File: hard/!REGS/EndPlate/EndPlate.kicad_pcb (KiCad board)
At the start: 2 copper layers, 99.1 x 68.6 mm, 39 parts, among them J1 Conn_01x13_Socket, J10 Conn_01x03_Pin, J11 Conn_01x09_Pin, J12 Conn_01x09_Pin, J13 Conn_01x09_Pin, J14 Conn_01x09_Pin, J15 Conn_01x01_Pin, J16 Conn_01x01_Pin, J17 Screw_Terminal_01x02, J2 Conn_01x13_Socket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

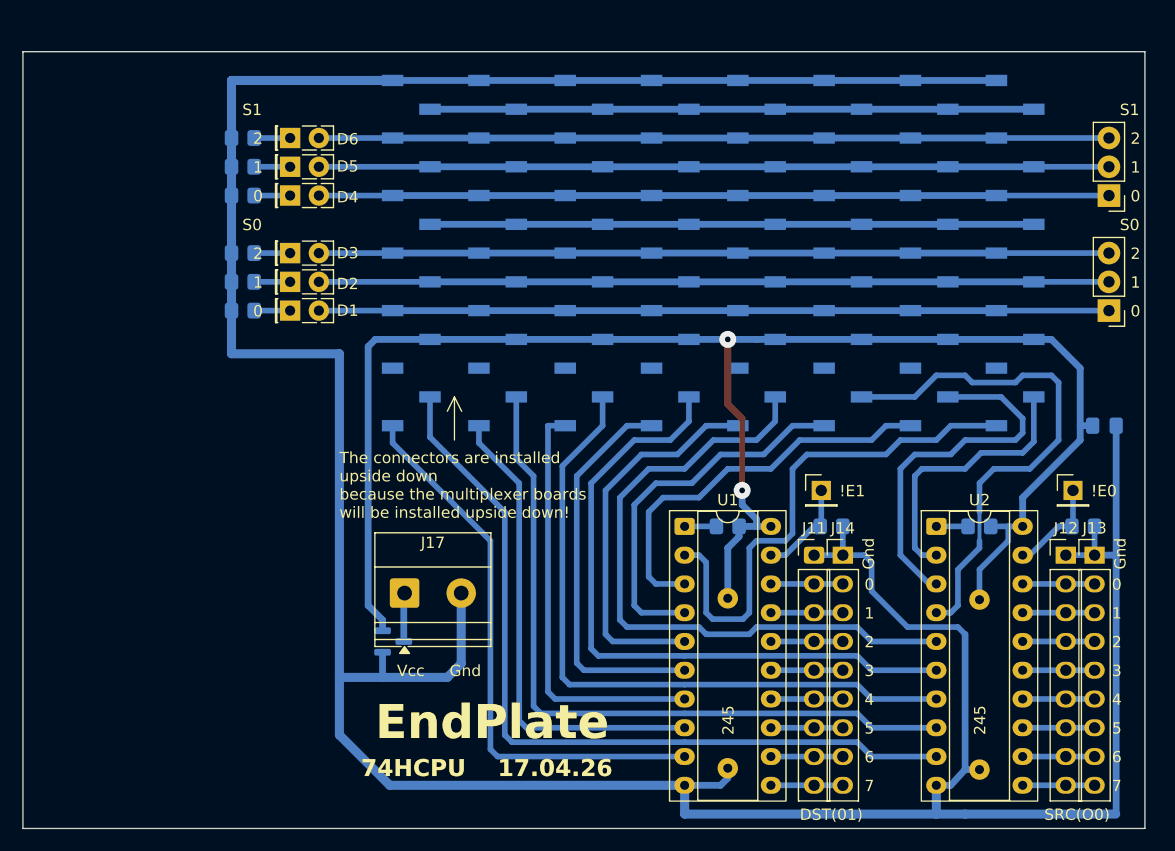
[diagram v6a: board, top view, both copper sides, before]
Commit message: Cut EndPlate PCB
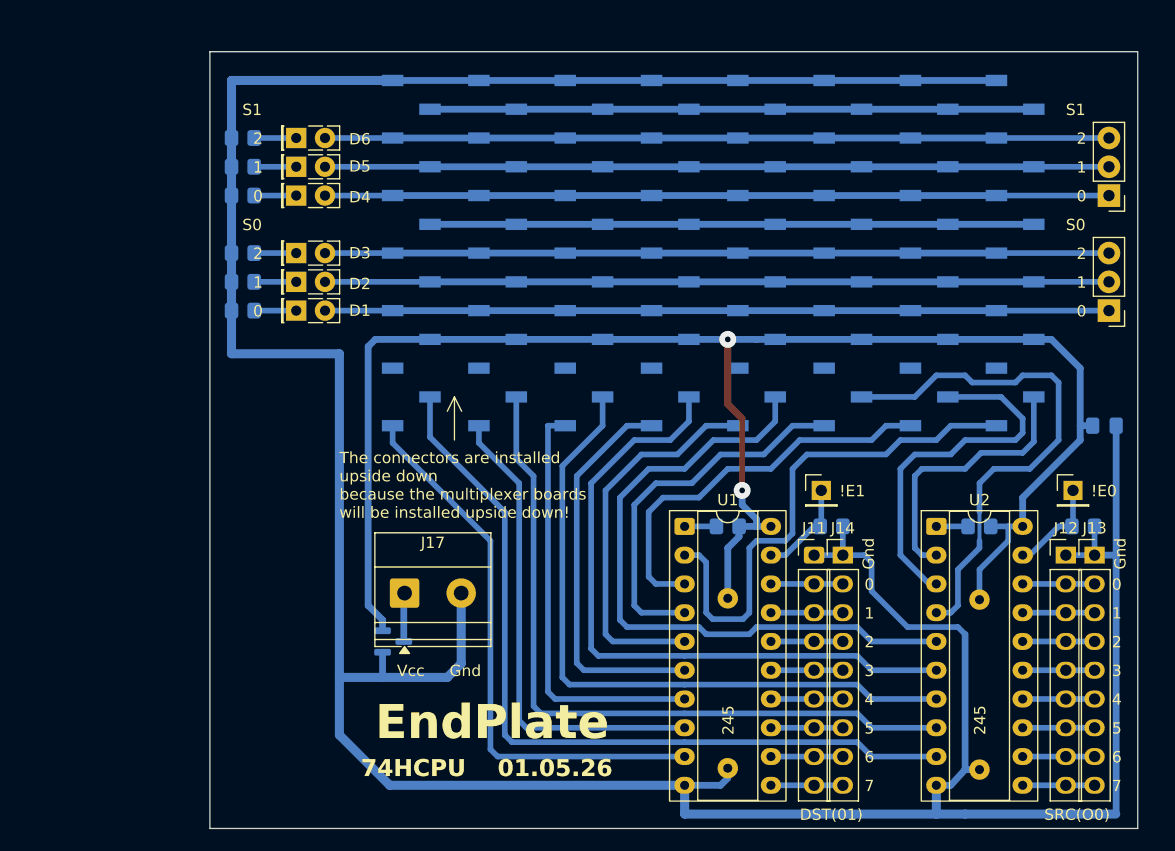
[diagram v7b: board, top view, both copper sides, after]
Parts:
- moved D1 0.54 mm to (55.9, 45.7)
- moved D2 0.54 mm to (55.9, 43.2)
- moved D3 0.54 mm to (55.9, 40.6)
- moved D4 0.54 mm to (55.9, 35.6)
- moved D5 0.54 mm to (55.9, 33.0)
- moved D6 0.54 mm to (55.9, 30.5)
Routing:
- net /S1.2: track 69.8 -> 69.2 mm
- net /S0.0: track 69.8 -> 69.2 mm
- net Net-(D6-K): track 3.18 -> 3.72 mm
- net Net-(D5-K): track 3.18 -> 3.72 mm
- net Net-(D4-K): track 3.18 -> 3.72 mm
- net Net-(D3-K): track 3.18 -> 3.72 mm
- net Net-(D2-K): track 3.18 -> 3.72 mm
- net Net-(D1-K): track 3.18 -> 3.72 mm
- net /S1.1: track 69.8 -> 69.2 mm
- net /S1.0: track 69.8 -> 69.2 mm
- net /S0.2: track 69.8 -> 69.2 mm
- net /S0.1: track 69.8 -> 69.2 mm
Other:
- board size 99.1 x 68.6 mm -> 81.9 x 68.6 mm
- board text added: "01.05.26"
- board text removed: "17.04.26"
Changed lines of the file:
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@@
 		)
 		(property "Value" "Conn_01x03_Pin"
-			(at -1.905 3.81 90)
+			(at 3.81 3.175 90)
 			(layer "F.Fab")
 			(effects
@@
 		)
 		(property "Value" "Conn_01x03_Pin"
-			(at -1.905 0 90)
+			(at 3.81 2.54 90)
 			(layer "F.Fab")
 			(effects
@@
 	(footprint "LED_THT:LED_Rectangular_W5.0mm_H2.0mm"
 		(layer "F.Cu")
-		(at 55.34 30.48)
+		(at 55.88 30.48)
 		(descr "LED, Rectangular, size 5.0x2.0mm, 2 pins, http://www.kingbright.com/attachments/file/psearch/000/00/00/L-169XCGDK(Ver.9B).pdf, generated by kicad-footprint-generator")
 		(tags "LED")
 		(property "Reference" "D6"
-			(at 5.08 0.1025 0)
+			(at 5.62 0.1025 0)
 			(layer "F.SilkS")
 			(effects
@@
 	(footprint "LED_THT:LED_Rectangular_W5.0mm_H2.0mm"
 		(layer "F.Cu")
-		(at 55.34 35.56)
+		(at 55.88 35.56)
 		(descr "LED, Rectangular, size 5.0x2.0mm, 2 pins, http://www.kingbright.com/attachments/file/psearch/000/00/00/L-169XCGDK(Ver.9B).pdf, generated by kicad-footprint-generator")
 		(tags "LED")
 		(property "Reference" "D4"
-			(at 5.08 0.14 0)
+			(at 5.62 0.14 0)
 			(layer "F.SilkS")
 			(effects
@@
 	(footprint "LED_THT:LED_Rectangular_W5.0mm_H2.0mm"
 		(layer "F.Cu")
-		(at 55.34 43.18)
+		(at 55.88 43.18)
 		(descr "LED, Rectangular, size 5.0x2.0mm, 2 pins, http://www.kingbright.com/attachments/file/psearch/000/00/00/L-169XCGDK(Ver.9B).pdf, generated by kicad-footprint-generator")
 		(tags "LED")
 		(property "Reference" "D2"
-			(at 5.08 0.1775 0)
+			(at 5.62 0.1775 0)
 			(layer "F.SilkS")
 			(effects
@@
 	(footprint "LED_THT:LED_Rectangular_W5.0mm_H2.0mm"
 		(layer "F.Cu")
-		(at 55.34 45.72)
+		(at 55.88 45.72)
 		(descr "LED, Rectangular, size 5.0x2.0mm, 2 pins, http://www.kingbright.com/attachments/file/psearch/000/00/00/L-169XCGDK(Ver.9B).pdf, generated by kicad-footprint-generator")
 		(tags "LED")
 		(property "Reference" "D1"
-			(at 5.08 0 0)
+			(at 5.62 0 0)
 			(layer "F.SilkS")
 			(effects
@@
 	(footprint "LED_THT:LED_Rectangular_W5.0mm_H2.0mm"
 		(layer "F.Cu")
-		(at 55.34 33.02)
+		(at 55.88 33.02)
 		(descr "LED, Rectangular, size 5.0x2.0mm, 2 pins, http://www.kingbright.com/attachments/file/psearch/000/00/00/L-169XCGDK(Ver.9B).pdf, generated by kicad-footprint-generator")
 		(tags "LED")
 		(property "Reference" "D5"
-			(at 5.08 -0.0375 0)
+			(at 5.62 -0.0375 0)
 			(layer "F.SilkS")
 			(effects
@@
 	(footprint "LED_THT:LED_Rectangular_W5.0mm_H2.0mm"
 		(layer "F.Cu")
-		(at 55.34 40.64)
+		(at 55.88 40.64)
 		(descr "LED, Rectangular, size 5.0x2.0mm, 2 pins, http://www.kingbright.com/attachments/file/psearch/000/00/00/L-169XCGDK(Ver.9B).pdf, generated by kicad-footprint-generator")
 		(tags "LED")
 		(property "Reference" "D3"
-			(at 5.08 0 0)
+			(at 5.62 0 0)
 			(layer "F.SilkS")
 			(effects
@@
 		(tags "resistor handsolder")
 		(property "Reference" "R6"
-			(at 2.81 0 0)
+			(at -2.4925 0 90)
 			(layer "B.SilkS")
 			(effects
@@
 		(tags "resistor handsolder")
 		(property "Reference" "R10"
-			(at 3.445 0 0)
+			(at -2.4925 0 90)
 			(layer "B.SilkS")
 			(effects
@@
 		(tags "resistor handsolder")
 		(property "Reference" "R8"
-			(at 2.81 -0.04 0)
+			(at -2.4925 0 90)
 			(layer "B.SilkS")
 			(effects
@@
 		(tags "resistor handsolder")
 		(property "Reference" "R5"
-			(at 2.905 0 0)
+			(at -2.4925 0 90)
 			(layer "B.SilkS")
 			(effects
@@
 		(tags "resistor handsolder")
 		(property "Reference" "R9"
-			(at 2.81 0 0)
+			(at -2.4925 0 90)
 			(layer "B.SilkS")
 			(effects
@@
 		(tags "resistor handsolder")
 		(property "Reference" "R7"
-			(at 2.81 0 0)
+			(at -2.4925 0 90)
 			(layer "B.SilkS")
 			(effects
@@
 	)
 	(gr_line
-		(start 130.81 91.44)
-		(end 31.75 91.44)
+		(start 130.175 91.44)
+		(end 48.26 91.44)
 		(stroke
 			(width 0.05)
@@
 	)
 	(gr_line
-		(start 130.81 22.86)
-		(end 130.81 91.44)
+		(start 130.175 22.86)
+		(end 130.175 91.44)
 		(stroke
 			(width 0.05)
@@
 	)
 	(gr_line
-		(start 31.75 22.86)
-		(end 130.81 22.86)
+		(start 48.26 22.86)
+		(end 130.175 22.86)
 		(stroke
 			(width 0.05)
@@
 	)
 	(gr_line
-		(start 31.75 91.44)
-		(end 31.75 22.86)
+		(start 48.26 91.44)
+		(end 48.26 22.86)
 		(stroke
 			(width 0.05)
@@
 		)
 	)
-	(gr_text "17.04.26"
+	(gr_text "01.05.26"
 		(at 73.66 86.995 0)
 		(layer "F.Cu")
@@
 	)
 	(gr_text "2"
-		(at 129.54 41.275 0)
+		(at 124.7775 41.275 0)
 		(layer "F.SilkS")
 		(effects
@@
 	)
 	(gr_text "1"
-		(at 129.54 43.815 0)
+		(at 124.7775 43.815 0)
 		(layer "F.SilkS")
 		(effects
@@
 		)
 	)
-	(gr_text "17.04.26"
+	(gr_text "01.05.26"
 		(at 73.66 86.995 0)
 		(layer "F.SilkS")
@@
 	)
 	(gr_text "0"
-		(at 129.54 36.195 0)
+		(at 124.7775 36.195 0)
 		(layer "F.SilkS")
 		(effects
@@
 	)
 	(gr_text "2"
-		(at 129.54 31.115 0)
+		(at 124.7775 31.115 0)
 		(layer "F.SilkS")
 		(effects
@@
 	)
 	(gr_text "1"
-		(at 129.54 33.655 0)
+		(at 124.7775 33.655 0)
 		(layer "F.SilkS")
 		(effects
@@
 	)
 	(gr_text "S0"
-		(at 128.5875 38.735 0)
+		(at 123.825 38.735 0)
 		(layer "F.SilkS")
 		(effects
@@
 	)
 	(gr_text "0"
-		(at 129.54 46.355 0)
+		(at 124.7775 46.355 0)
 		(layer "F.SilkS")
 		(effects
@@
 	)
 	(gr_text "S1"
-		(at 128.5875 28.575 0)
+		(at 123.825 28.575 0)
 		(layer "F.SilkS")
 		(effects
@@
 	)
 	(segment
-		(start 57.88 35.56)
+		(start 58.42 35.56)
 		(end 64.39 35.56)
 		(width 0.5)
@@
 	)
 	(segment
-		(start 57.88 43.18)
+		(start 58.42 43.18)
 		(end 67.69 43.18)
 		(width 0.5)
@@
 	)
 	(segment
-		(start 57.88 33.02)
+		(start 58.42 33.02)
 		(end 67.69 33.02)
 		(width 0.5)
@@
 	)
 	(segment
-		(start 57.88 30.48)
+		(start 58.42 30.48)
 		(end 64.39 30.48)
 		(width 0.5)
@@
 	)
 	(segment
-		(start 57.88 40.64)
+		(start 58.42 40.64)
 		(end 64.39 40.64)
 		(width 0.5)
@@
 	)
 	(segment
-		(start 57.88 45.72)
+		(start 58.42 45.72)
 		(end 64.39 45.72)
 		(width 0.5)
@@
 	)
 	(segment
-		(start 55.34 45.72)
+		(start 55.88 45.72)
 		(end 52.165 45.72)
 		(width 0.5)
@@
 	)
 	(segment
-		(start 55.34 43.18)
+		(start 55.88 43.18)
 		(end 52.165 43.18)
 		(width 0.5)
@@
 	)
 	(segment
-		(start 55.34 40.64)
+		(start 55.88 40.64)
 		(end 52.165 40.64)
 		(width 0.5)
@@
 	)
 	(segment
-		(start 55.34 35.56)
+		(start 55.88 35.56)
 		(end 52.165 35.56)
 		(width 0.5)
@@
 	)
 	(segment
-		(start 55.34 33.02)
+		(start 55.88 33.02)
 		(end 52.165 33.02)
 		(width 0.5)
@@
 	)
 	(segment
-		(start 55.34 30.48)
+		(start 55.88 30.48)
 		(end 52.165 30.48)
 		(width 0.5)
